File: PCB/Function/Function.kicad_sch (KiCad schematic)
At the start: 12 parts

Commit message: Update Function.kicad_sch
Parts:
- removed J**11, J**12: Pomona_1581, 5Y:Pomona-1581, symbol 5Y:Pomona_1581
- added C1, C2, C3, C4: 4u7, symbol Device:C
- added C5: 100n, symbol Device:C
- added D1: LED5, symbol 5Y:LED5
- added J1, J2: Conn_01x03, symbol Connector_Generic:Conn_01x03
- added R1: 4K7, Resistor_SMD:R_1206_3216Metric, symbol Device:R
- added R2: 680K, Resistor_SMD:R_1206_3216Metric, symbol Device:R
- added R3, R5: 10K, Resistor_SMD:R_1206_3216Metric, symbol Device:R
- added R4, R6, R7: 100K, Resistor_SMD:R_1206_3216Metric, symbol Device:R
- added U1: AD823, symbol 5Y:AD823
- added U2: LM4040DBZ-5, Package_TO_SOT_SMD:SOT-23, symbol Reference_Voltage:LM4040DBZ-5
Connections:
- new net: D1.1 (K), R1.2, U1.6 (-)
- new net: D1.2 (A), U1.7
- new net: R3.1, R4.2
- new net: R2.1, R3.2, U1.3 (+)
- new net: R6.1, R7.2, U1.2 (-)
- new net GND: C1.2, C2.1, C3.2, C4.1, C5.2, J1.2 (Pin_2), J2.2 (Pin_2), R1.1, R4.1, R6.2, U1.4 (V-), U2.2 (A)
- new net LP: U1.5 (+)
- new net REF: R5.1, R7.1, U2.1 (K)
- new net TRIG: R2.2, U1.1
- new net VCC: C1.1, C3.1, C5.1, J1.3 (Pin_3), J2.3 (Pin_3), R5.2, U1.8 (V+)
- new net VEE: C2.2, C4.2, J1.1 (Pin_1), J2.1 (Pin_1)
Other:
- moved on the sheet: J**1, J**10, J**2, J**3, J**4, J**5, J**6, J**7, J**8, J**9

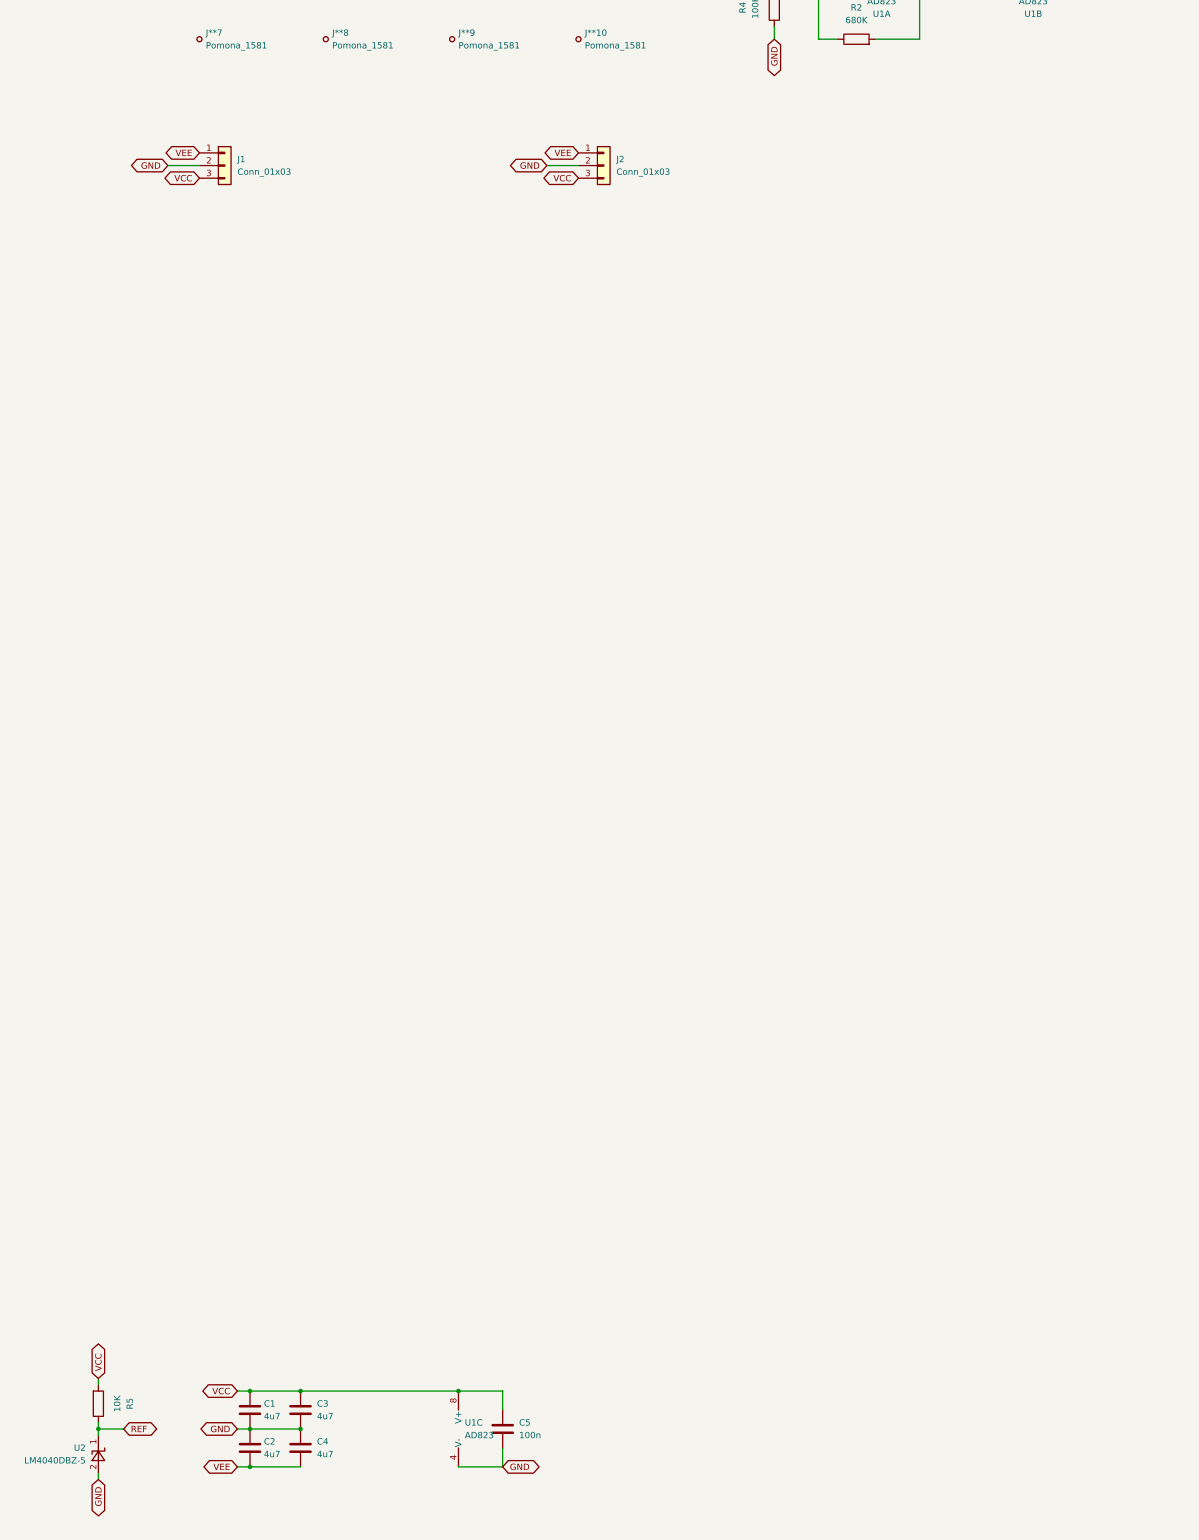
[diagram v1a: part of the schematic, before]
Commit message: Add flip-flop, END, LIM
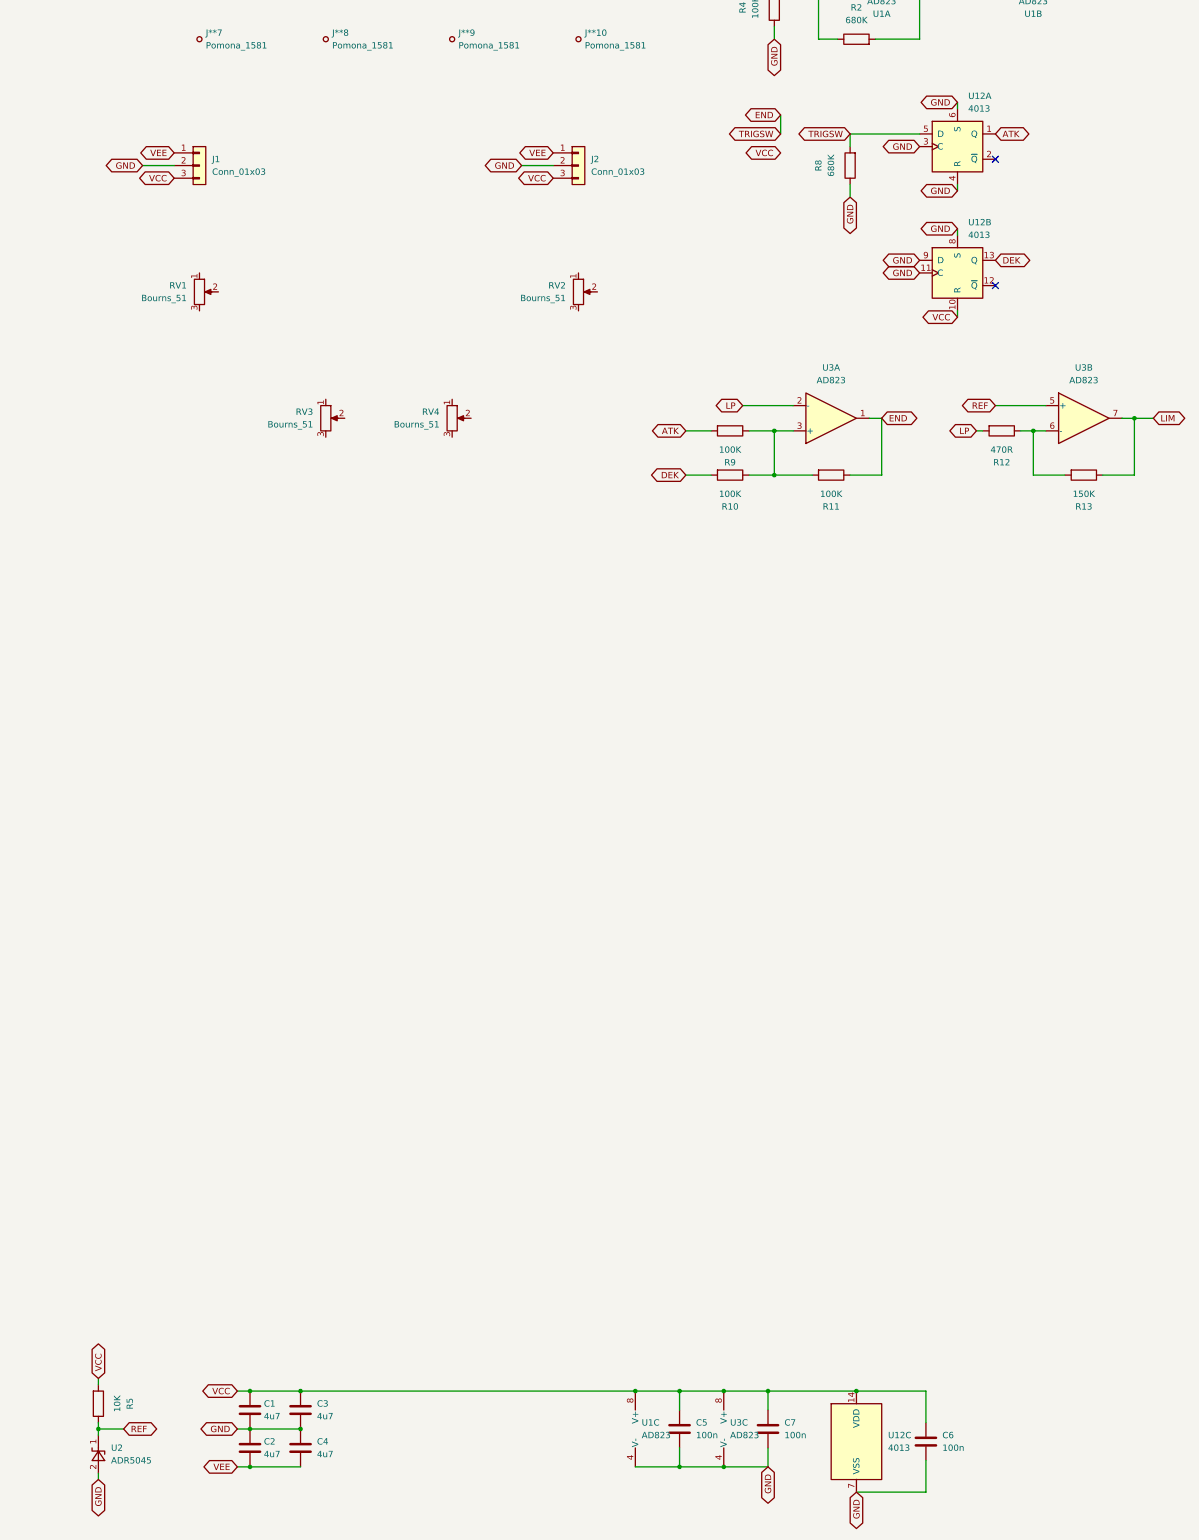
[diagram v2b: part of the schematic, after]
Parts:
- removed U2: LM4040DBZ-5, Package_TO_SOT_SMD:SOT-23, symbol Reference_Voltage:LM4040DBZ-5
- added C6, C7: 100n, symbol Device:C
- added R10, R11, R9: 100K, Resistor_SMD:R_1206_3216Metric, symbol Device:R
- added R12: 470R, Resistor_SMD:R_1206_3216Metric, symbol Device:R
- added R13: 150K, Resistor_SMD:R_1206_3216Metric, symbol Device:R
- added R8: 680K, Resistor_SMD:R_1206_3216Metric, symbol Device:R
- added RV1, RV2, RV3, RV4: Bourns_51, symbol 5Y:Bourns_51
- added U12: 4013, Package_SO:SOIC-14_3.9x8.7mm_P1.27mm, symbol 5Y:4013
- added U2: ADR5045, Package_TO_SOT_SMD:SOT-23, symbol 5Y:ADR5045
- added U3: AD823, 5Y:SOIC-8, symbol 5Y:AD823
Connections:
- net GND: now also C6.2, C7.2, R8.1, U12.11 (C), U12.3 (C), U12.4 (R), U12.6 (S), U12.7 (VSS), U12.8 (S), U12.9 (D), U2.2 (A), U3.4 (V-)
- net LP: now also R12.2, U3.2 (-)
- net REF: now also U2.1 (K), U3.5 (+)
- net VCC: now also C6.1, C7.1, U12.10 (R), U12.14 (VDD), U3.8 (V+)
- new net: R12.1, R13.2, U3.6 (-)
- new net: R10.1, R11.2, R9.1, U3.3 (+)
- new net ATK: R9.2, U12.1 (Q)
- new net DEK: R10.2, U12.13 (Q)
- new net END: R11.1, R8.2, U12.5 (D), U3.1
- new net LIM: R13.1, U3.7
- no-connect marks 0 -> 2
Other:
- moved on the sheet: C5, J1, J2, U1C

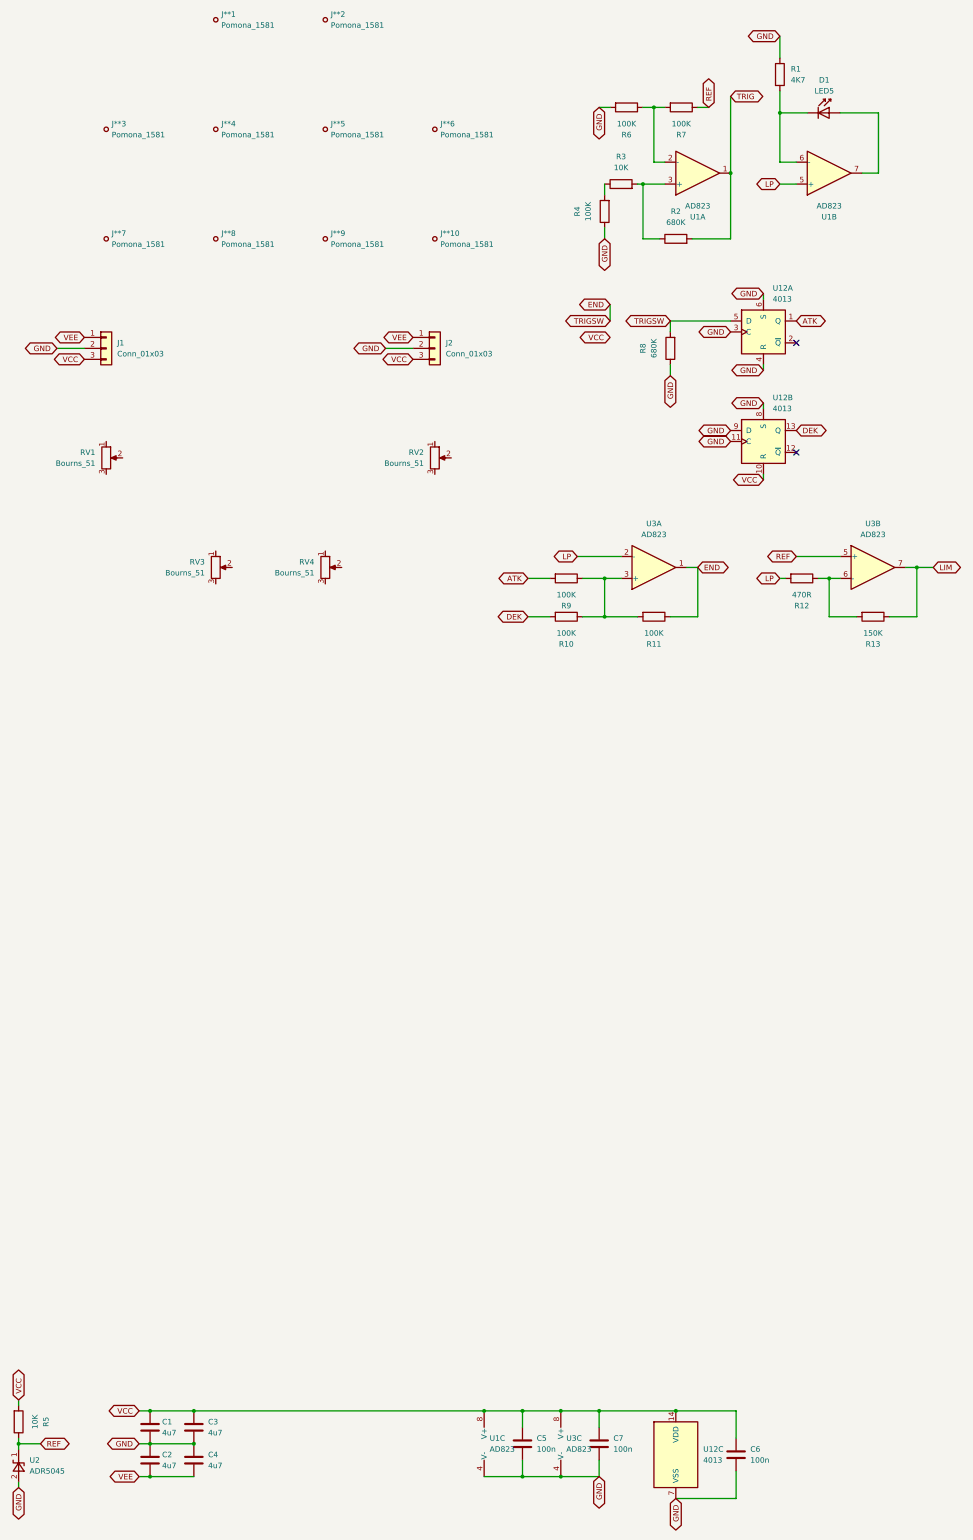
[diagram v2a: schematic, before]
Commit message: Update simulation
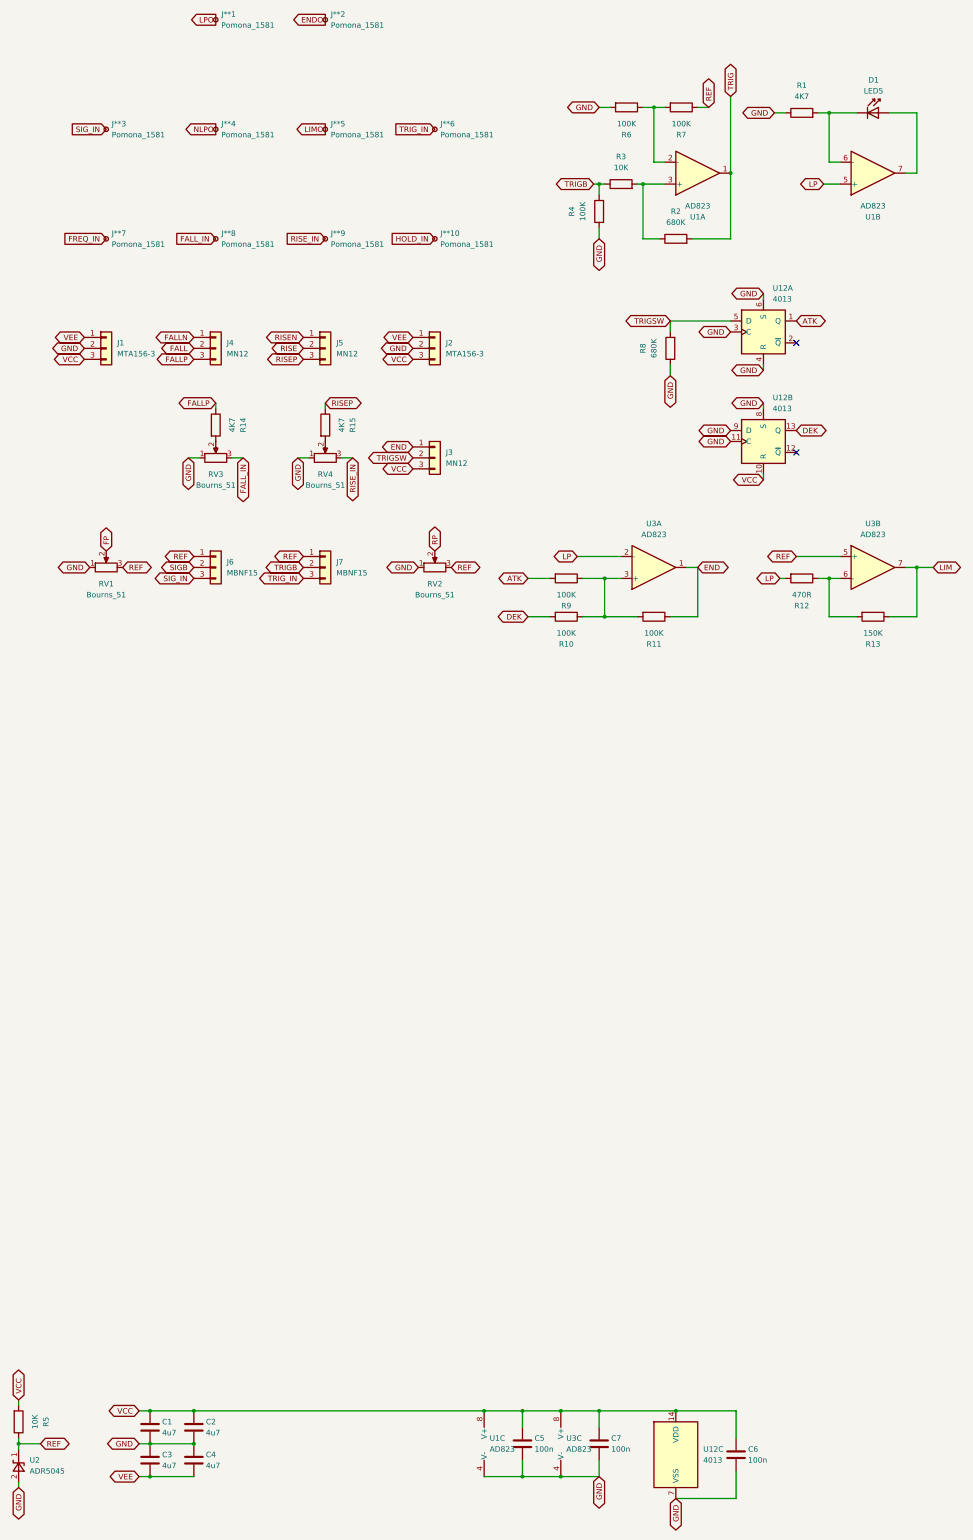
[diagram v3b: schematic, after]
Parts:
- removed J1, J2: Conn_01x03, symbol Connector_Generic:Conn_01x03
- added J1, J2: MTA156-3, 5Y:MTA156-3, symbol 5Y:MTA156-3
- added J3, J4, J5: MN12, 5Y:MBNF15, symbol 5Y:MN12
- added J6, J7: MBNF15, 5Y:MBNF15, symbol 5Y:MBNF15
- added R14, R15: 4K7, Resistor_SMD:R_1206_3216Metric, symbol Device:R
- C1, C2, C3, C4, C5, C6, C7: footprint (none) -> Capacitor_SMD:C_1206_3216Metric
- RV1, RV2, RV3, RV4: footprint (none) -> 5Y:Bourns_51
- U1: footprint (none) -> 5Y:SOIC-8
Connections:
- net END: now also J3.1 (Pin_1); no longer R8.2, U12.5 (D)
- net GND: now also C2.2, C3.1, RV1.1, RV2.1, RV3.1, RV4.1, J1.2 (Pin_2), J2.2 (Pin_2); no longer C2.1, C3.2
- net REF: now also RV1.3, RV2.3, J6.1 (Pin_1), J7.1 (Pin_1)
- net VCC: now also C2.1, J1.3 (Pin_3), J2.3 (Pin_3), J3.3 (Pin_3); no longer C3.1
- net VEE: now also C3.2, J1.1 (Pin_1), J2.1 (Pin_1); no longer C2.2
- net ENDO: now reaches J**2.1
- net RP: now reaches RV2.2
- net LPO: now reaches J**1.1
- net SIG_IN: now reaches J**3.1
- net SIG_IN: now also J6.3 (Pin_3)
- net TRIGB: now reaches R3.1, R4.2
- net TRIGB: now also J7.2 (Pin_2)
- net FREQ_IN: now reaches J**7.1
- net FP: now reaches RV1.2
- net NLPO: now reaches J**4.1
- net at RV4.2: now also R15.2
- net RISE_IN: now reaches RV4.3
- net RISE_IN: now also J**9.1
- net FALL_IN: now reaches J**8.1
- net FALL_IN: now also RV3.3
- net HOLD_IN: now reaches J**10.1
- net TRIG_IN: now reaches J**6.1
- net TRIG_IN: now also J7.3 (Pin_3)
- net LIMO: now reaches J**5.1
- net at RV3.2: now also R14.2
- new net FALL: J4.2 (Pin_2)
- new net FALLN: J4.1 (Pin_1)
- new net FALLP: J4.3 (Pin_3), R14.1
- new net RISE: J5.2 (Pin_2)
- new net RISEN: J5.1 (Pin_1)
- new net RISEP: J5.3 (Pin_3), R15.1
- new net SIGB: J6.2 (Pin_2)
- new net TRIGSW: J3.2 (Pin_2), R8.2, U12.5 (D)
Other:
- moved on the sheet: D1, R1, R4, RV1, RV2, RV3, RV4, U1B

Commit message: Update Function schematic
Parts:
- removed J2: MTA156-3, 5Y:MTA156-3, symbol 5Y:MTA156-3
- added C10, C11, C12, C13, C14, C15, C16, C17, C22, C23, C24, C25, C26, C27, C28, C29, C30, C8, C9: 100n, Capacitor_SMD:C_1206_3216Metric, symbol Device:C
- added C18, C19, C20, C21, C31, C32, C33, C34, C35: 47p, Capacitor_SMD:C_1206_3216Metric, symbol Device:C
- added J2: MTA156-3-PWR, 5Y:MTA156-3, symbol 5Y:MTA156-3-PWR
- added Q1: BC847, Package_TO_SOT_SMD:SOT-23-6, symbol 5Y:BCM847
- added Q2: BCM857, Package_TO_SOT_SMD:SOT-23-6, symbol 5Y:BCM857
- added R16, R47, R49: 4K7, Resistor_SMD:R_1206_3216Metric, symbol Device:R
- added R17, R39, R40: 150K, Resistor_SMD:R_1206_3216Metric, symbol Device:R
- added R18: 6M8, Resistor_SMD:R_1206_3216Metric, symbol Device:R
- added R19, R21, R24, R27, R29, R30, R31, R32, R34, R35, R36, R37: 47K, Resistor_SMD:R_1206_3216Metric, symbol Device:R
- added R20, R28, R33, R38: 470, Resistor_SMD:R_1206_3216Metric, symbol Device:R
- added R22, R25, R50, R51, R52, R53, R54, R57, R58, R60, R63, R66, R69: 100K, Resistor_SMD:R_1206_3216Metric, symbol Device:R
- added R23, R26, R41, R43: 33K, Resistor_SMD:R_1206_3216Metric, symbol Device:R
- added R42, R44, R46, R48, R59, R61, R62, R64, R65, R67, R68, R70: 68K, Resistor_SMD:R_1206_3216Metric, symbol Device:R
- added R45, R55: 10K, Resistor_SMD:R_1206_3216Metric, symbol Device:R
- added R56: 680K, Resistor_SMD:R_1206_3216Metric, symbol Device:R
- added U10, U3, U4, U5, U6, U7, U8, U9: AD823, 5Y:SOIC-8, symbol 5Y:AD823
- added U11: ADG419, Package_SO:SOIC-8_3.9x4.9mm_P1.27mm, symbol 5Y:ADG419
- R10: value 100K -> 68K
- R12: value 470R -> 4K7
- renumbered U2 to U15, U3 to U2
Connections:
- net ATK: now also R51.2
- net DEK: now also R52.2; no longer R10.2
- net END: now also R22.1
- net ENDO: now also R19.2, R20.1
- net FALLN: now also R66.2
- net FALLP: now also R69.2; no longer R14.1
- net FP: now also U10.3 (+)
- net GND: now also R10.2, C10.2, C11.1, C12.2, C13.1, C14.2, C15.1, C16.2, C17.1, C23.2, C24.1, C25.2, C26.1, C27.2, C28.1, C29.2, C30.1, C8.2, C9.1, J2.2 (Pin_2), Q1.2 (B), Q1.6 (C), Q2.2 (B), Q2.6 (C), R17.1, R23.1, R26.1, R31.1, R34.1, R36.1, R39.1, R40.1, R42.1, R53.2, R54.2, R58.1, U11.3 (GND), U5.5 (+), U6.3 (+), U6.5 (+), U7.3 (+), U7.5 (+)
- net HOLD_IN: now also R54.1, R55.2
- net LIM: now also R25.1
- net LIMO: now also R27.2, R28.1
- net LP: now also C22.2, R21.1, R24.1, R29.1, R35.1, R43.1, U5.7
- net LPO: now also R37.2, R38.1
- net NLPO: now also R32.2, R33.1
- net REF: now also R16.2, R30.1, R57.2, R61.2, R67.2; no longer U2.5 (+)
- net RISEN: now also R60.2
- net RISEP: now also R63.2; no longer R15.1
- net RP: now also U9.5 (+)
- net SIGB: now also R41.2
- net VCC: now also C10.1, C12.1, C14.1, C16.1, C23.1, C25.1, C27.1, C29.1, C8.1, J2.3 (Pin_3), R18.1, U10.8 (V+), U11.4 (V+), U11.5 (VL), U3.8 (V+), U4.8 (V+), U5.8 (V+), U6.8 (V+), U7.8 (V+), U8.8 (V+), U9.8 (V+)
- net VEE: now also C11.2, C13.2, C15.2, C17.2, C24.2, C26.2, C28.2, C30.2, C9.2, J2.1 (Pin_1), U10.4 (V-), U11.7 (V-), U3.4 (V-), U4.4 (V-), U5.4 (V-), U6.4 (V-), U7.4 (V-), U8.4 (V-), U9.4 (V-)
- net at R10.1, R11.2, R9.1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: now also R18.2
- net FALL renamed FAB
- net FAB: now also U10.6 (-), U10.7
- net FREQ_IN renamed FREQ
- net FREQ: now also R62.2, R68.2
- net RISE renamed RAB
- net RAB: now also U9.1, U9.2 (-)
- new net: R41.1, R42.2, U5.2 (-)
- new net: R57.1, R58.2, U8.6 (-)
- new net: C34.1, R48.2, R62.1, R63.1, R64.1, U6.6 (-)
- new net: R52.1, R53.1, U8.3 (+)
- new net: R43.2, R44.1, U5.3 (+)
- new net: C19.1, R24.2, R27.1, U3.6 (-)
- new net: R55.1, R56.2, U8.5 (+)
- new net: R25.2, R26.2, R39.2, U3.5 (+)
- new net: C32.1, R46.2, R66.1, R67.1, U7.2 (-)
- new net: C21.1, R34.2, R37.1, U4.2 (-)
- new net: C21.2, R38.2, U4.1
- new net: C18.1, R19.1, R21.2, U3.2 (-)
- new net: C20.2, R33.2, U4.7
- new net: C33.1, R47.2, R65.1, R68.1, R69.1, R70.1, U7.6 (-)
- new net: R35.2, R36.2, U4.3 (+)
- new net: C35.1, R49.2, R59.1, R60.1, R61.1, U6.2 (-)
- new net: R16.1, R17.2, U2.5 (+)
- new net: Q1.3 (C), Q2.3 (C), U11.1
- new net: C22.1, U11.2, U5.6 (-)
- new net: R30.2, R31.2, U4.5 (+)
- new net: C20.1, R29.2, R32.1, U4.6 (-)
- new net: C31.1, R50.2, R51.1, U8.2 (-)
- new net: R22.2, R23.2, R40.2, U3.3 (+)
- new net: C18.2, R20.2, U3.1
- new net: R45.2, U5.1
- new net: Q1.1 (E), Q1.4 (E), Q2.1 (E), Q2.4 (E), R45.1
- new net: C19.2, R28.2, U3.7
- new net DRV: C31.2, R44.2, R50.1, U8.1
- new net FAP: R14.1, U10.5 (+)
- new net FB: R70.2, U10.1, U10.2 (-)
- new net HOLD: R56.1, U11.6, U8.7
- new net NVFF: C32.2, R46.1, R65.2, U7.1
- new net NVRF: C35.2, Q1.5 (B), R49.1, U6.1
- new net RAP: R15.1, U9.3 (+)
- new net RB: R64.2, U9.6 (-), U9.7
- new net VFF: C33.2, Q2.5 (B), R47.1, U7.7
- new net VRF: C34.2, R48.1, R59.2, U6.7
- no-connect marks 2 -> 3
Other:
- moved on the sheet: C5, C6, C7, D1, R1, R10, R11, R12, R13, R2, R3, R4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

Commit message: Start placement
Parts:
- C22: value 100n -> 4n7
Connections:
- net DRV: now also R44.1; no longer R44.2
- net LP: now also R43.2; no longer R43.1
- net REF: now also R18.1
- net VCC: no longer R18.1
- new net: R43.1, R44.2, U5.3 (+)
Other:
- moved on the sheet: C31, C32, C33, C34, C35, R10, R11, R12, R13, R16, R17, R18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
